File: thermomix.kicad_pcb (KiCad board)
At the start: 4 copper layers, 61.5 x 33.4 mm, 65 parts, among them J101 DX07S016JA1R1500, J102 Conn_01x05, J201 Conn_02x12_Odd_Even, SW101 SW_Push, SW102 SW_Push, U101 MIC5353-3.3YMT, U102 TPD2E2U06, U103 STM32F303RDTx, U201 LTC2983, Y101 Crystal_GND24

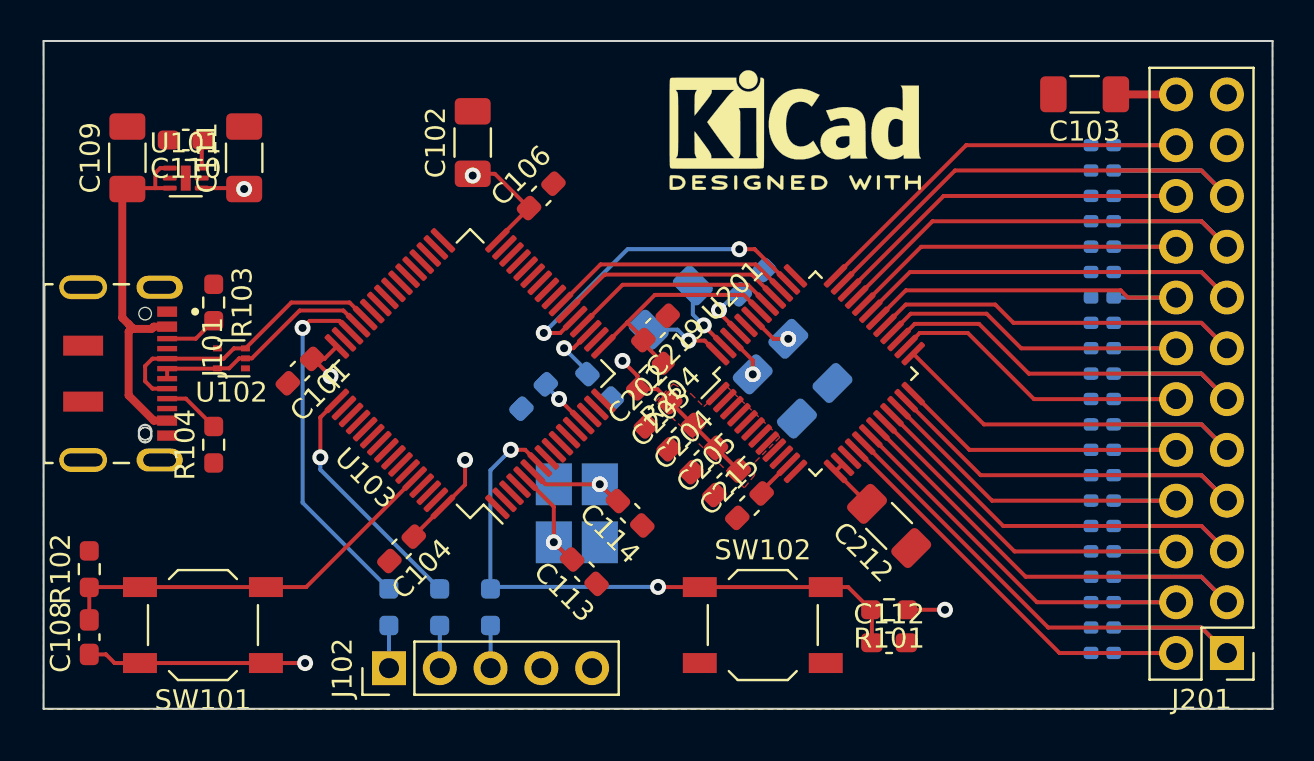
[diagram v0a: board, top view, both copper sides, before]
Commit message: Silk-screen done
Signed-off-by: Alexis Jeandet <alexis.jeandet@member.fsf.org>
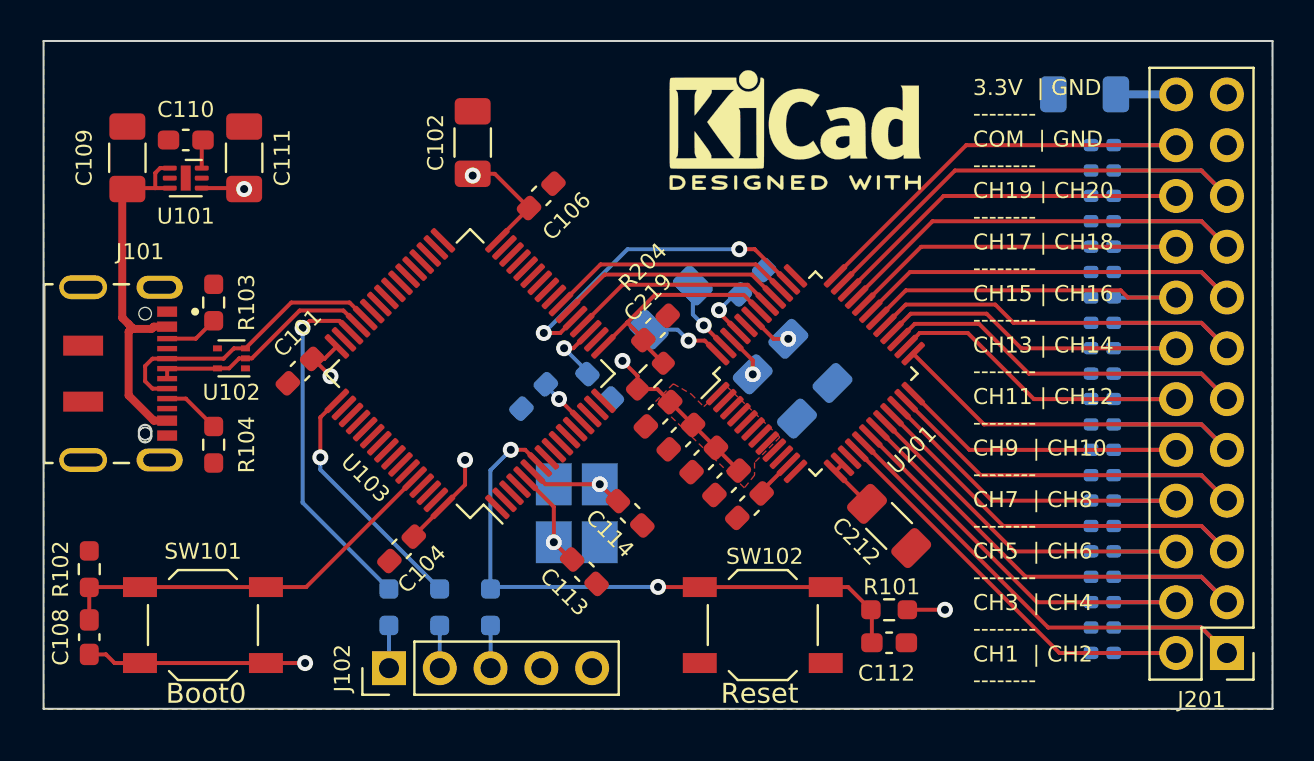
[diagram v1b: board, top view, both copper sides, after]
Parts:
- C103: moved to B.Cu
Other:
- board text added: "3.3V | GND -------- COM | GND -------- CH19 | CH20 -------- CH17 | CH18 -------- CH15 | CH16 -------- CH13 | CH14 -------- CH11 | CH12 -------- CH9 | CH10 -------- CH7 | CH8 -------- CH5 | CH6 -------- CH3 | CH4 -------- CH1 | CH2 --------"
- board text added: "Boot0"
- board text added: "Reset"

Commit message: Adds sdcard and battery
Signed-off-by: Alexis Jeandet <alexis.jeandet@member.fsf.org>
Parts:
- added BT101: Battery_Cell, Battery:BatteryHolder_Keystone_3000_1x12mm, B.Cu at (134.2, 79.4)
- added C115: 100nF, Capacitor_SMD:C_0603_1608Metric_Pad1.08x0.95mm_HandSolder, F.Cu at (115.6, 78.0)
- added J103: Micro_SD_Card_Det_Hirose_DM3AT, Connector_Card:microSD_HC_Hirose_DM3D-SF, B.Cu at (115.7, 81.2)
- added R108: 10k, Resistor_SMD:R_0603_1608Metric_Pad0.98x0.95mm_HandSolder, B.Cu at (107.7, 84.2)
- moved C102 7.46 mm to (124.7, 83.1), turned to 45 degrees
- moved C201 3.32 mm to (131.3, 89.0), turned to 45 degrees
- moved C208 1.59 mm to (126.8, 86.8)
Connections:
- U103 pad 1: unconnected-(U103-Pad1) -> /VBAT
- U103 pad 33: unconnected-(U103-Pad33) -> /SPI2_NSS
- U103 pad 34: unconnected-(U103-Pad34) -> /SPI2_SCK
- U103 pad 35: unconnected-(U103-Pad35) -> /SPI2_MISO
- U103 pad 36: unconnected-(U103-Pad36) -> /SPI2_MOSI
- U103 pad 37: unconnected-(U103-Pad37) -> /CARD_DETECT
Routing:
- net /VBAT: track 0.00 -> 39.6 mm, vias 0 -> 3
- net /SPI2_MOSI: track 0.00 -> 13.8 mm, vias 0 -> 1
- net /SPI2_MISO: track 0.00 -> 10.2 mm, vias 0 -> 1
- net /SPI2_SCK: track 0.00 -> 9.09 mm, vias 0 -> 1
- net /CARD_DETECT: track 0.00 -> 8.52 mm, vias 0 -> 1
- net /SPI2_NSS: track 0.00 -> 8.20 mm, vias 0 -> 1
- net /3.3V: track 49.5 -> 54.0 mm, vias 10 -> 11
- net Net-(C208-Pad2): track 3.95 -> 5.65 mm
- net Net-(C208-Pad1): track 3.72 -> 4.71 mm
- net /TH_RESET: track 12.6 -> 12.0 mm
- net GND: vias 0 -> 22

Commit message: 1.0 release
Signed-off-by: Alexis Jeandet <alexis.jeandet@member.fsf.org>
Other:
- board text added: "Thermomix 1.0"
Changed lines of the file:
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@@
     (effects (font (size 0.8 0.8) (thickness 0.15)) (justify left))
+  )
+  (gr_text "Thermomix 1.0" (at 134.6708 82.8548) (layer "F.SilkS")
+    (effects (font (size 1.2 1.2) (thickness 0.2)))
   )
   (gr_text "Boot0" (at 105.029 99.314) (layer "F.SilkS")

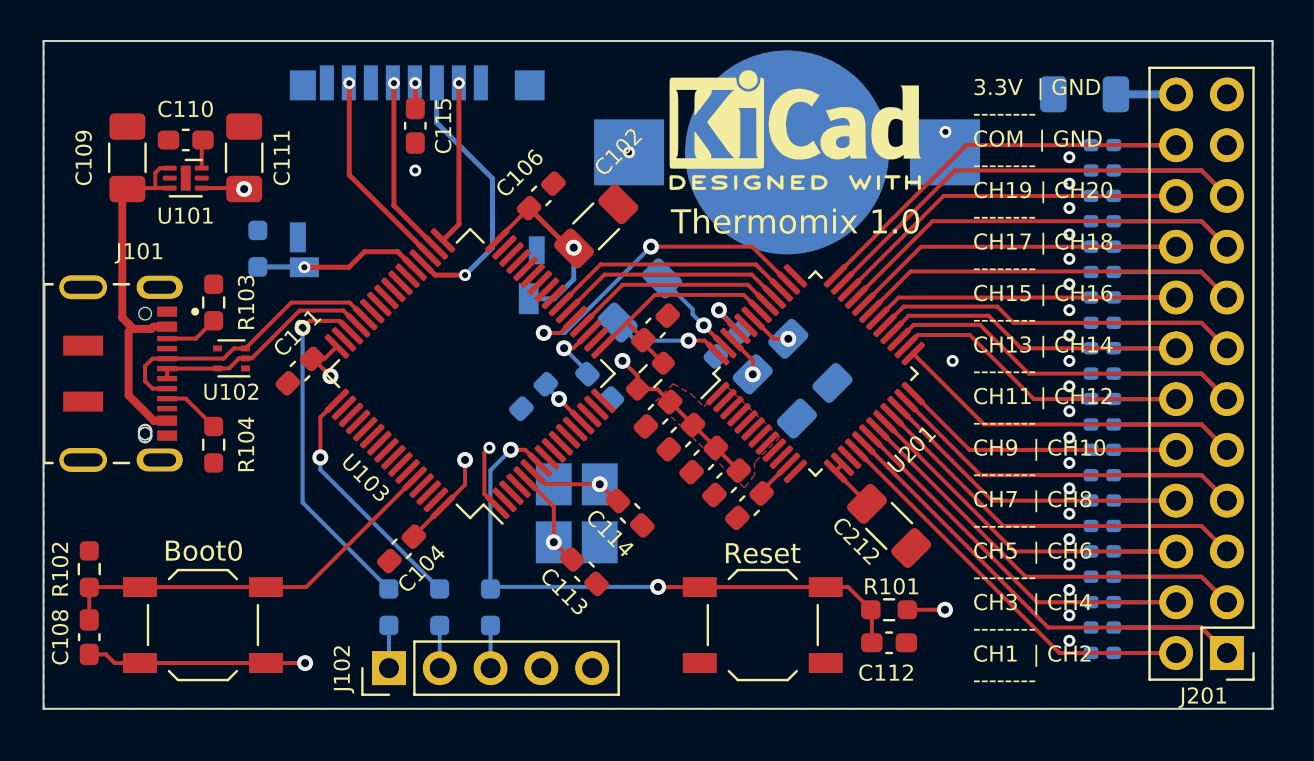
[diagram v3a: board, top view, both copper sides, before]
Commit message: Fixes bugs from 1.0
Signed-off-by: Alexis Jeandet <alexis.jeandet@member.fsf.org>
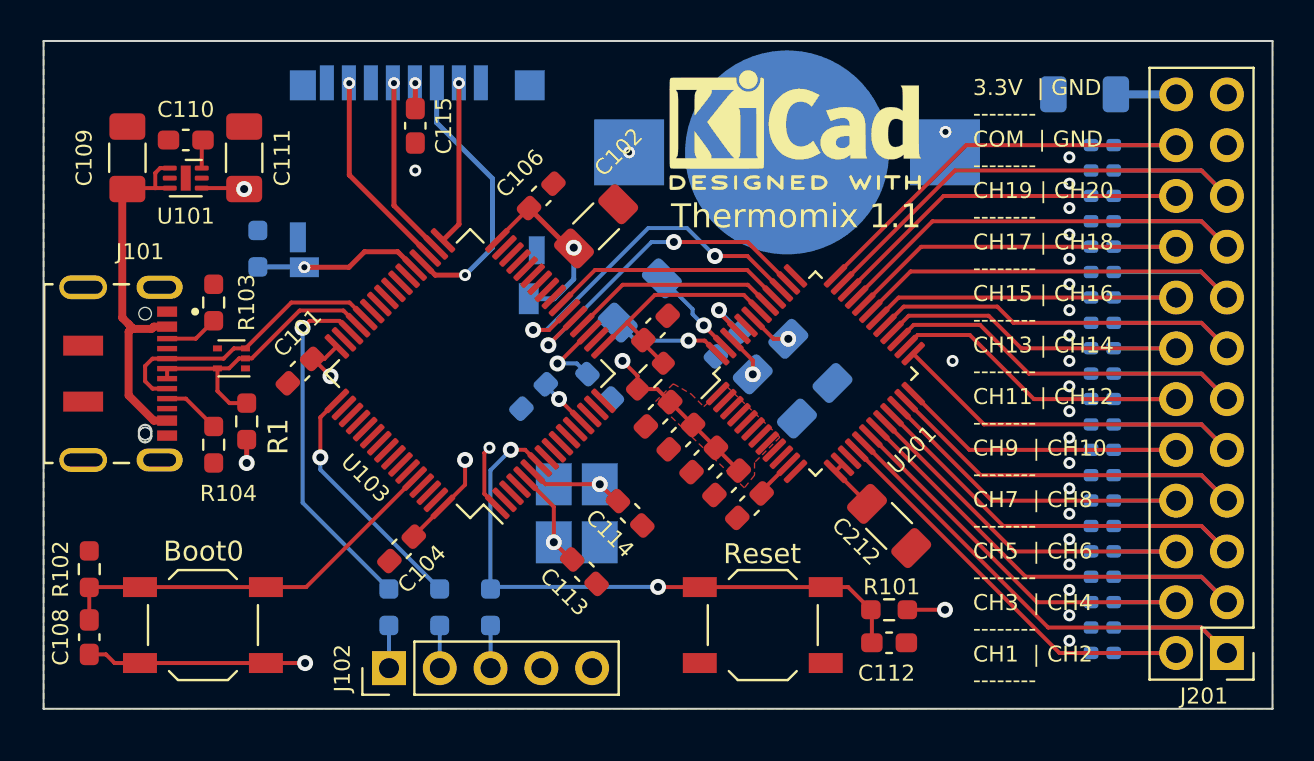
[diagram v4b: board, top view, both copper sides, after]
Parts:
- added R1: 1.5k, Resistor_SMD:R_0603_1608Metric_Pad0.98x0.95mm_HandSolder, F.Cu at (107.2, 92.8)
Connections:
- U102 pad 2: /USB_D+ -> unconnected-(U102-Pad2)
- U103 pad 22: /SPI1_MOSI -> /SPI1_MISO
- U103 pad 23: /SPI1_MISO -> /SPI1_MOSI
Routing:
- net /SPI1_MISO: track 12.4 -> 17.9 mm, vias 0 -> 2
- net /USB_D+: track 11.6 -> 14.4 mm
- net /3.3V: track 54.0 -> 55.8 mm, vias 11 -> 12
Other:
- board text added: "Thermomix 1.1"
- board text removed: "Thermomix 1.0"
